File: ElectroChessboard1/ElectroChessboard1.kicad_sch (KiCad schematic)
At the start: 19 parts, among them IC75 DS1307Z+T&R, J3 Conn_01x04_Pin, J5 Conn_01x06, J6 Conn_01x06, U1 ATmega2560-16A, U2 1027, Y1 Crystal, Y3 Crystal

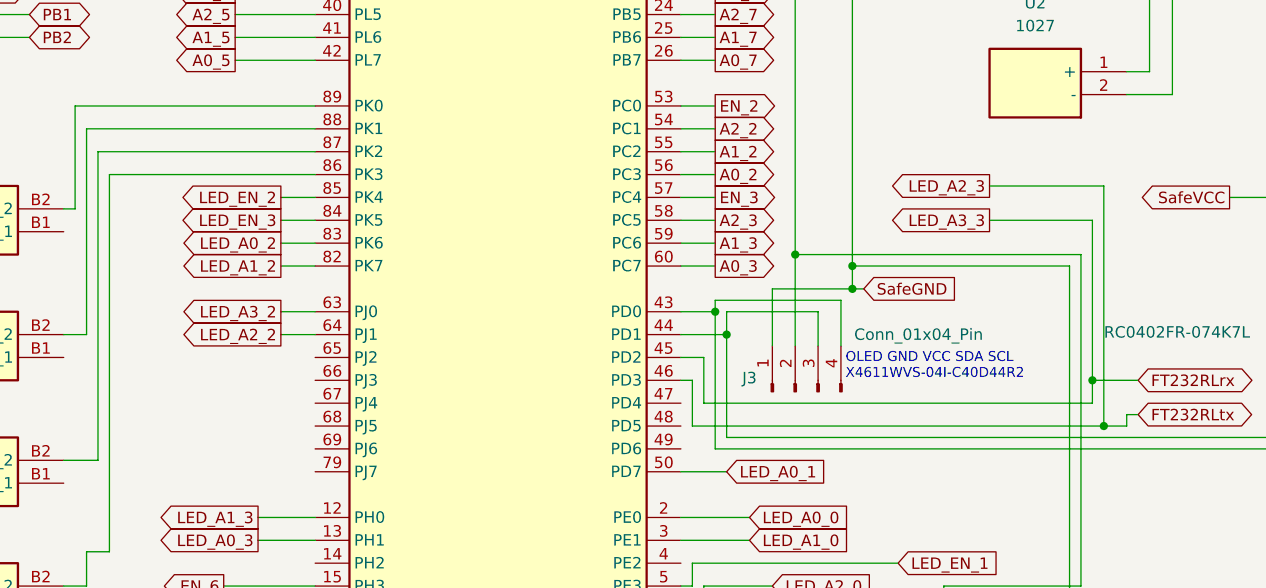
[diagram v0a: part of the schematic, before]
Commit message: Chessboard done
Other parts left to place. Also, I changed some wiring in schematic, changing what was connected to RX TX1
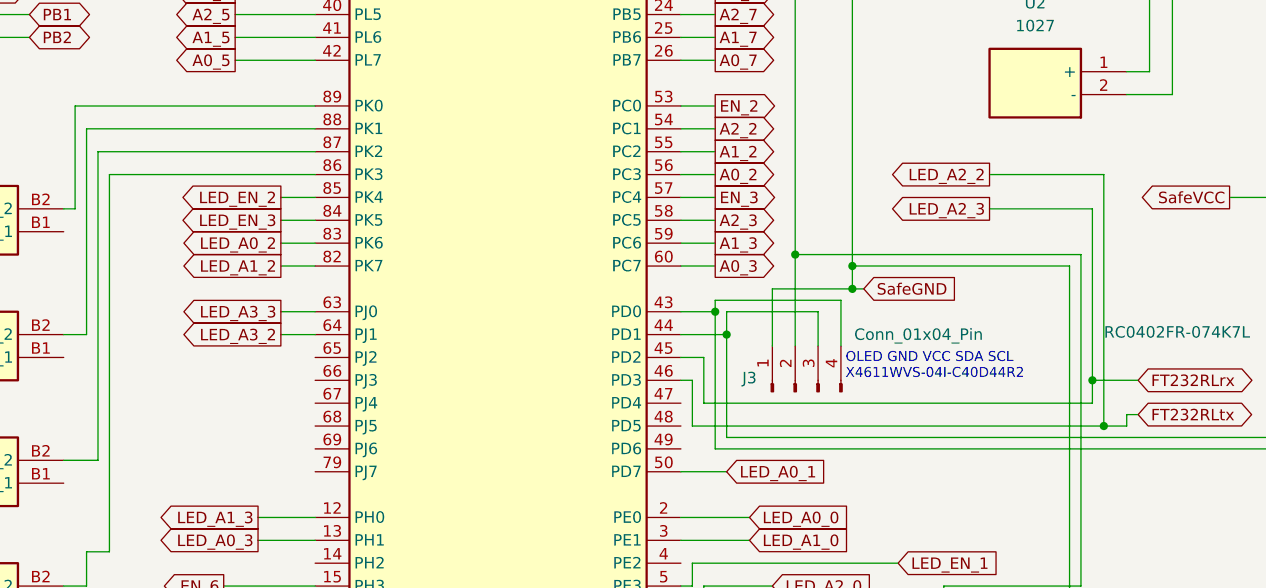
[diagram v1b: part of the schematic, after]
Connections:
- net LED_A2_2 is gone; now on net LED_A3_2: U1.64 (PJ1)
- net LED_A3_2: no longer U1.63 (PJ0)
- new net LED_A3_3: U1.63 (PJ0)
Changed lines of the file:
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@@
 	(wire
 		(pts
-			(xy 99.06 106.68) (xy 102.87 106.68)
-		)
-		(stroke
-			(width 0)
-			(type default)
-		)
-	)
-	(wire
-		(pts
 			(xy 93.98 58.42) (xy 102.87 58.42)
 		)
@@
 	(wire
 		(pts
-			(xy 190.5 90.17) (xy 190.5 116.84)
-		)
-		(stroke
-			(width 0)
-			(type default)
-		)
-	)
-	(wire
-		(pts
 			(xy 143.51 43.18) (xy 147.32 43.18)
 		)
@@
 	(wire
 		(pts
-			(xy 177.8 90.17) (xy 190.5 90.17)
+			(xy 189.23 92.71) (xy 189.23 111.76)
 		)
 		(stroke
@@
 	(wire
 		(pts
-			(xy 177.8 93.98) (xy 189.23 93.98)
+			(xy 146.05 134.62) (xy 146.05 137.16)
 		)
 		(stroke
@@
 	(wire
 		(pts
-			(xy 146.05 134.62) (xy 146.05 137.16)
+			(xy 210.82 91.44) (xy 240.03 91.44)
 		)
 		(stroke
@@
 	(wire
 		(pts
-			(xy 210.82 91.44) (xy 240.03 91.44)
+			(xy 60.96 38.1) (xy 60.96 36.83)
 		)
 		(stroke
@@
 	(wire
 		(pts
-			(xy 60.96 38.1) (xy 60.96 36.83)
+			(xy 83.82 38.1) (xy 87.63 38.1)
 		)
 		(stroke
@@
 	(wire
 		(pts
-			(xy 83.82 38.1) (xy 87.63 38.1)
+			(xy 43.18 109.22) (xy 46.99 109.22)
 		)
 		(stroke
@@
 	(wire
 		(pts
-			(xy 43.18 109.22) (xy 46.99 109.22)
+			(xy 144.78 134.62) (xy 144.78 132.08)
 		)
 		(stroke
@@
 	(wire
 		(pts
-			(xy 144.78 134.62) (xy 144.78 132.08)
+			(xy 240.03 119.38) (xy 252.73 119.38)
 		)
 		(stroke
@@
 	(wire
 		(pts
-			(xy 240.03 119.38) (xy 252.73 119.38)
+			(xy 99.06 104.14) (xy 102.87 104.14)
 		)
 		(stroke
@@
 	(wire
 		(pts
+			(xy 190.5 88.9) (xy 190.5 116.84)
+		)
+		(stroke
+			(width 0)
+			(type default)
+		)
+	)
+	(wire
+		(pts
 			(xy 210.82 91.44) (xy 210.82 95.25)
 		)
@@
 	(wire
 		(pts
+			(xy 177.8 88.9) (xy 190.5 88.9)
+		)
+		(stroke
+			(width 0)
+			(type default)
+		)
+	)
+	(wire
+		(pts
 			(xy 143.51 81.28) (xy 147.32 81.28)
 		)
@@
 	(wire
 		(pts
+			(xy 99.06 106.68) (xy 102.87 106.68)
+		)
+		(stroke
+			(width 0)
+			(type default)
+		)
+	)
+	(wire
+		(pts
 			(xy 43.18 90.17) (xy 43.18 95.25)
 		)
@@
 	(wire
 		(pts
-			(xy 162.56 62.23) (xy 198.12 62.23)
+			(xy 177.8 92.71) (xy 189.23 92.71)
 		)
 		(stroke
@@
 	(wire
 		(pts
-			(xy 93.98 71.12) (xy 102.87 71.12)
+			(xy 162.56 62.23) (xy 198.12 62.23)
 		)
 		(stroke
@@
 	(wire
 		(pts
-			(xy 162.56 101.6) (xy 163.83 101.6)
+			(xy 93.98 71.12) (xy 102.87 71.12)
 		)
 		(stroke
@@
 	(wire
 		(pts
-			(xy 189.23 93.98) (xy 189.23 111.76)
+			(xy 162.56 101.6) (xy 163.83 101.6)
 		)
 		(stroke
@@
 	(wire
 		(pts
-			(xy 99.06 104.14) (xy 102.87 104.14)
-		)
-		(stroke
-			(width 0)
-			(type default)
-		)
-	)
-	(wire
-		(pts
 			(xy 156.21 97.79) (xy 156.21 24.13)
 		)
@@
 	(global_label "LED_A2_3"
 		(shape output)
-		(at 177.8 90.17 180)
+		(at 177.8 92.71 180)
 		(fields_autoplaced yes)
 		(effects
@@
 		)
 		(property "Intersheetrefs" "${INTERSHEET_REFS}"
-			(at 165.9249 90.17 0)
+			(at 165.9249 92.71 0)
 			(effects
 				(font
@@
 	(global_label "LED_A3_2"
 		(shape output)
-		(at 99.06 104.14 180)
+		(at 99.06 106.68 180)
 		(fields_autoplaced yes)
 		(effects
@@
 		)
 		(property "Intersheetrefs" "${INTERSHEET_REFS}"
-			(at 87.1849 104.14 0)
+			(at 87.1849 106.68 0)
 			(effects
 				(font
@@
 	(global_label "LED_A2_2"
 		(shape output)
-		(at 99.06 106.68 180)
+		(at 177.8 88.9 180)
 		(fields_autoplaced yes)
 		(effects
@@
 		)
 		(property "Intersheetrefs" "${INTERSHEET_REFS}"
-			(at 87.1849 106.68 0)
+			(at 165.9249 88.9 0)
 			(effects
 				(font
@@
 	(global_label "LED_A3_3"
 		(shape output)
-		(at 177.8 93.98 180)
+		(at 99.06 104.14 180)
 		(fields_autoplaced yes)
 		(effects
@@
 		)
 		(property "Intersheetrefs" "${INTERSHEET_REFS}"
-			(at 165.9249 93.98 0)
+			(at 87.1849 104.14 0)
 			(effects
 				(font

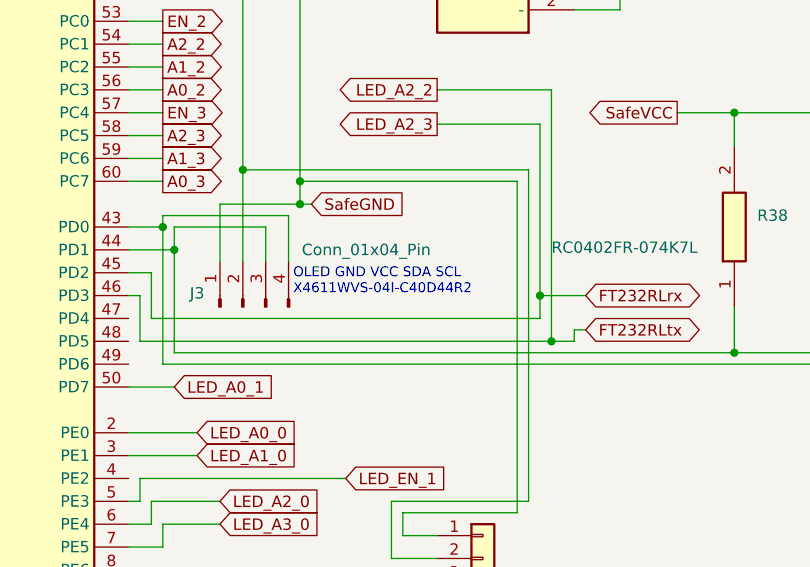
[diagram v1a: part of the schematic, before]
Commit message: Fixed pins
Now footprints of pins match
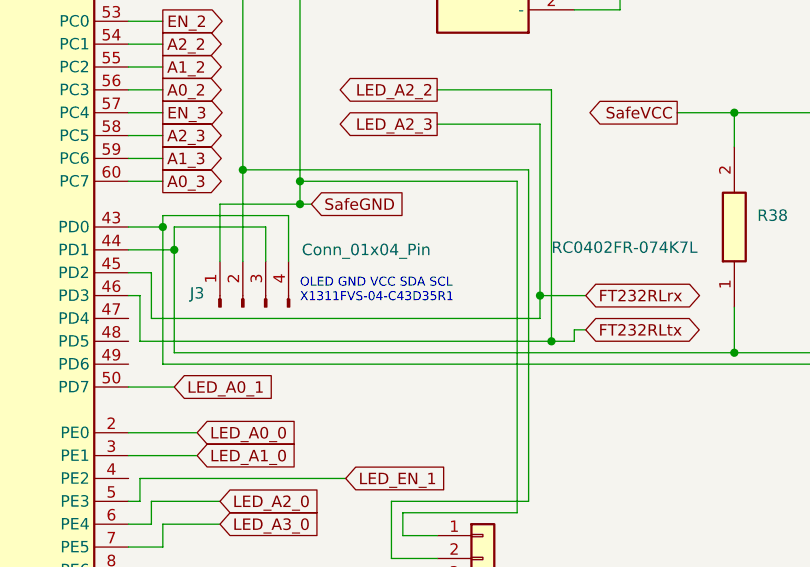
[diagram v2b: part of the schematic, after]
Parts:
- J3: footprint Connector_PinSocket_1.00mm:PinSocket_1x04_P1.00mm_Vertical_SMD_Pin1Left -> Connector_PinSocket_1.27mm:PinSocket_1x04_P1.27mm_Vertical_SMD_Pin1Right
- J5, J6: footprint Connector_PinSocket_1.00mm:PinSocket_1x06_P1.00mm_Vertical_SMD_Pin1Right -> Connector_PinSocket_2.00mm:PinSocket_1x06_P2.00mm_Vertical_SMD_Pin1Right
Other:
- note added: "OLED GND VCC SDA SCL X1311FVS-04-C43D35R1"
- note removed: "OLED GND VCC SDA SCL X4611WVS-04I-C40D44R2"
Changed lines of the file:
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@@
 		)
 	)
-	(text "OLED GND VCC SDA SCL\nX4611WVS-04I-C40D44R2"
+	(text "OLED GND VCC SDA SCL\nX1311FVS-04-C43D35R1"
 		(exclude_from_sim no)
-		(at 161.798 110.236 0)
+		(at 162.56 111.252 0)
 		(effects
 			(font
-				(size 1.1 1.1)
+				(size 1 1)
 			)
 			(justify left)
@@
 			)
 		)
-		(property "Footprint" "Connector_PinSocket_1.00mm:PinSocket_1x06_P1.00mm_Vertical_SMD_Pin1Right"
+		(property "Footprint" "Connector_PinSocket_2.00mm:PinSocket_1x06_P2.00mm_Vertical_SMD_Pin1Right"
 			(at 48.26 73.66 0)
 			(effects
@@
 			)
 		)
-		(property "Footprint" "Connector_PinSocket_1.00mm:PinSocket_1x06_P1.00mm_Vertical_SMD_Pin1Right"
+		(property "Footprint" "Connector_PinSocket_2.00mm:PinSocket_1x06_P2.00mm_Vertical_SMD_Pin1Right"
 			(at 182.88 143.51 0)
 			(effects
@@
 			)
 		)
-		(property "Footprint" "Connector_PinSocket_1.00mm:PinSocket_1x04_P1.00mm_Vertical_SMD_Pin1Left"
+		(property "Footprint" "Connector_PinSocket_1.27mm:PinSocket_1x04_P1.27mm_Vertical_SMD_Pin1Right"
 			(at 156.21 113.03 0)
 			(effects

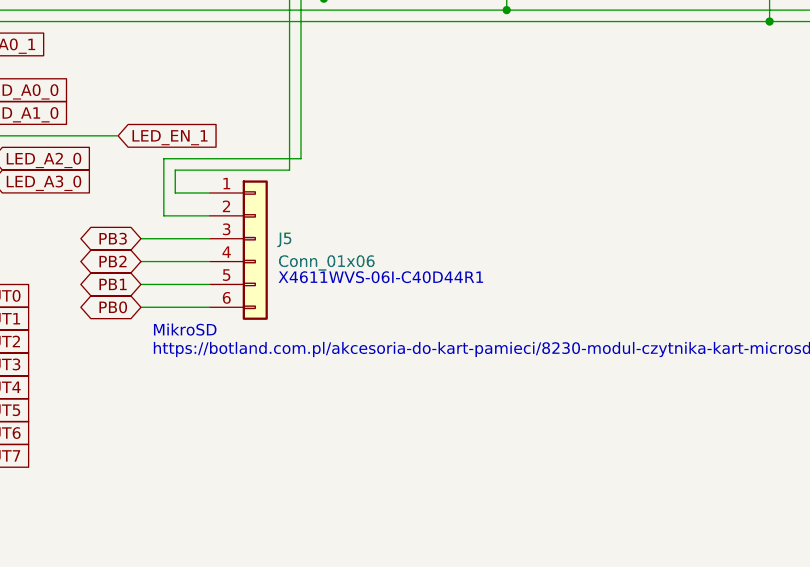
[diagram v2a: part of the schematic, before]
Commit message: Big part layout done
Microcontroller, mux/demux layout and of course wiring left. Also changed footprint of the SD card module pins.
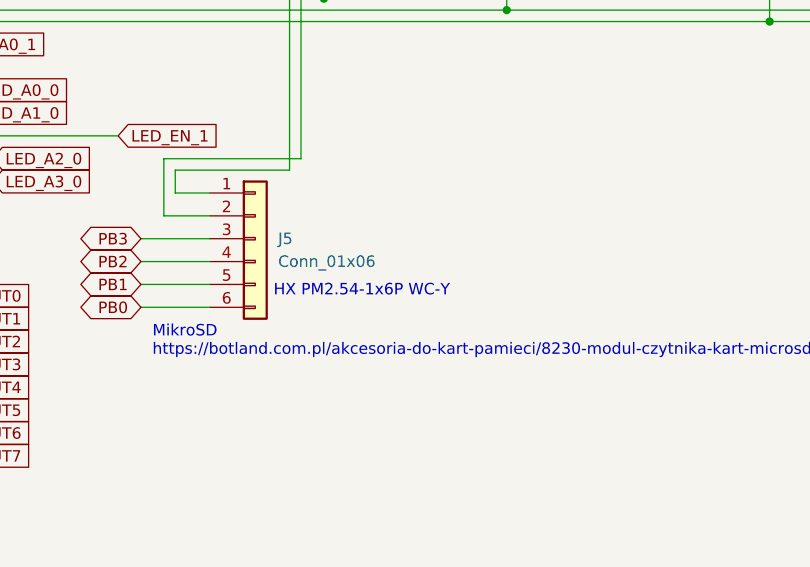
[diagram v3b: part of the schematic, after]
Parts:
- J5: footprint Connector_PinSocket_2.00mm:PinSocket_1x06_P2.00mm_Vertical_SMD_Pin1Right -> Connector_PinSocket_2.54mm:PinSocket_1x06_P2.54mm_Horizontal
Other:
- note added: "HX PM2.54-1x6P WC-Y"
- note removed: "X4611WVS-06I-C40D44R1"
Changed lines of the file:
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@@
 		)
 	)
-	(text "X4611WVS-06I-C40D44R1"
+	(text "HX PM2.54-1x6P WC-Y"
 		(exclude_from_sim no)
-		(at 185.42 148.082 0)
+		(at 184.912 149.352 0)
 		(effects
 			(font
@@
 			)
 		)
-		(property "Footprint" "Connector_PinSocket_2.00mm:PinSocket_1x06_P2.00mm_Vertical_SMD_Pin1Right"
+		(property "Footprint" "Connector_PinSocket_2.54mm:PinSocket_1x06_P2.54mm_Horizontal"
 			(at 182.88 143.51 0)
 			(effects

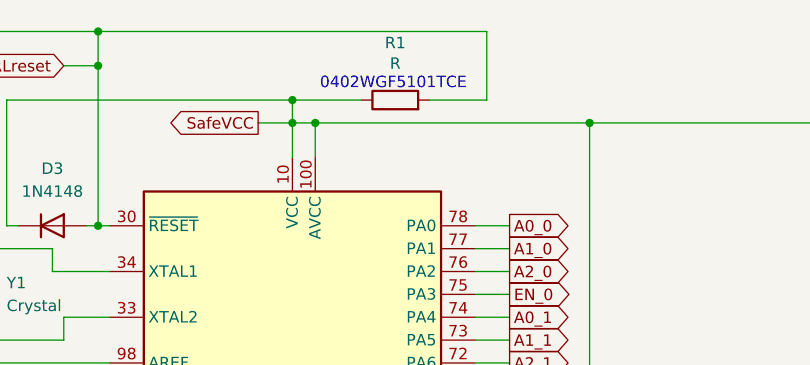
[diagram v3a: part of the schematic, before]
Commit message: Wired power, partially CPU too
.
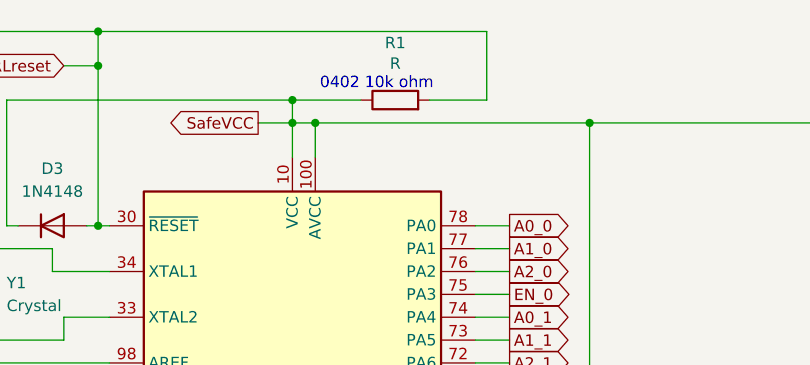
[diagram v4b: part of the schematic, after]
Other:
- note added: "0402 10k ohm"
- note removed: "0402WGF5101TCE"
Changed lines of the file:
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@@
 		)
 	)
-	(text "0402WGF5101TCE"
+	(text "0402 10k ohm"
 		(exclude_from_sim no)
 		(at 126.238 19.812 0)
